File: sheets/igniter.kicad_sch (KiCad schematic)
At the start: 18 parts, among them J18 Screw_Terminal_01x02, J19 Screw_Terminal_01x02, Q2 AO3400A, Q3 AO3400A

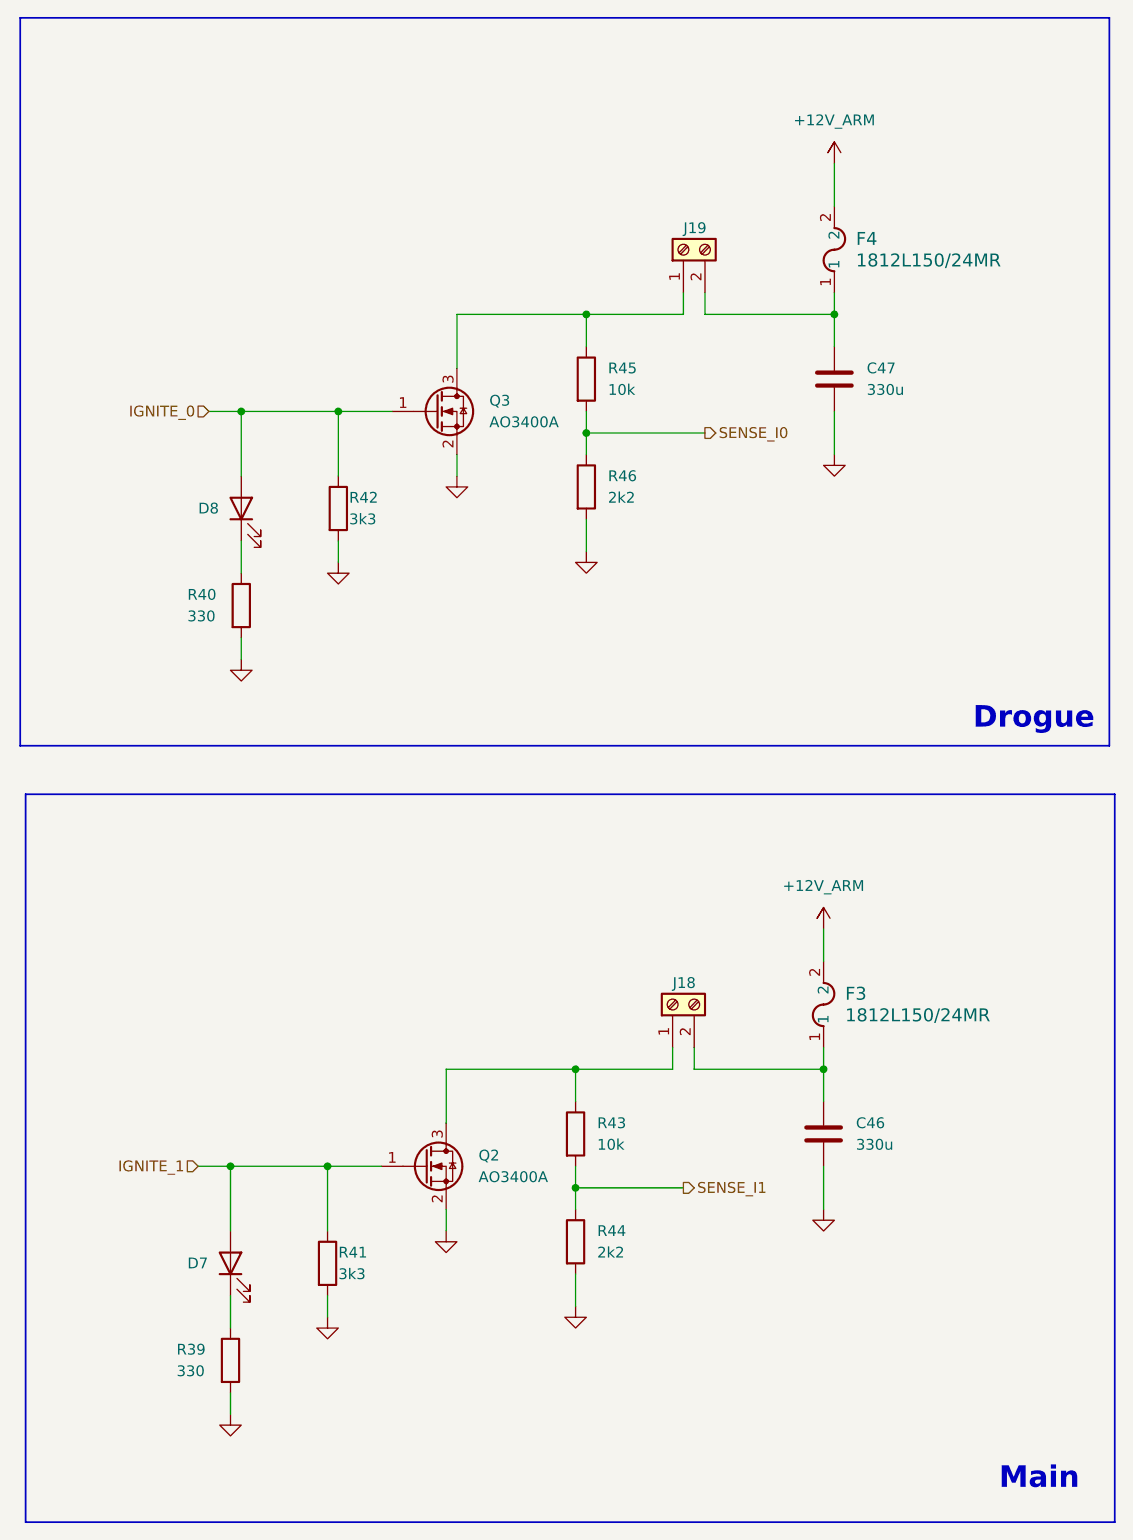
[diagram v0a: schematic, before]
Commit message: updated pyrocircuit with components and TO-252-2 footprint for mosfets. not done with sim
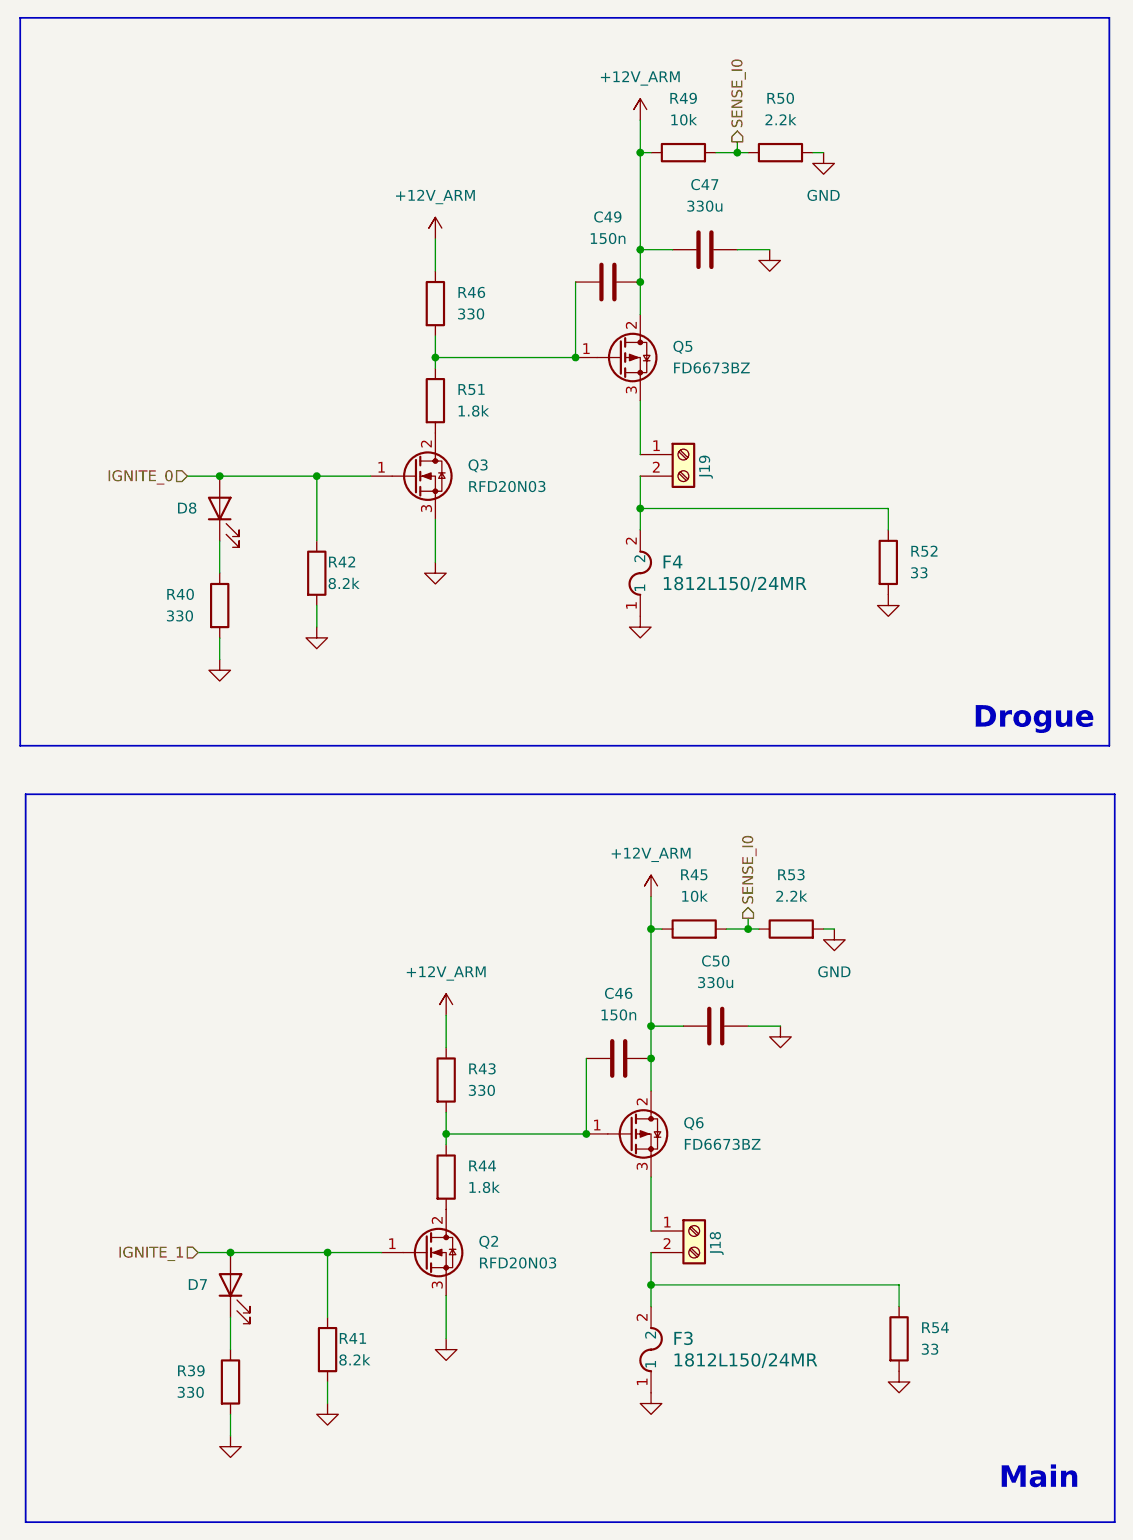
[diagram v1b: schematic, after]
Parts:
- removed Q2, Q3: AO3400A, Package_TO_SOT_SMD:SOT-23, symbol Transistor_FET:AO3400A
- added C49: 150n, symbol Device:C
- added C50: 330u, symbol Device:C
- added Q2, Q3: RFD20N03, Package_TO_SOT_SMD:TO-252-2, symbol Transistor_FET:Q_NMOS_GDS
- added Q5, Q6: FD6673BZ, Package_TO_SOT_SMD:TO-252-2, symbol Transistor_FET:Q_PMOS_GDS
- added R49: 10k, symbol Device:R
- added R50, R53: 2.2k, symbol Device:R
- added R51: 1.8k, symbol Device:R
- added R52, R54: 33, symbol Device:R
- C46: value 330u -> 150n
- R41, R42: value 3k3 -> 8.2k
- R43: value 10k -> 330
- R44: value 2k2 -> 1.8k
- R46: value 2k2 -> 330
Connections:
- net +12V_ARM: now also C46.1, C47.2, R43.1, R45.1, R46.1, C49.1, C50.2, Q5.2 (D), Q6.2 (D), R49.1; no longer F3.2, F4.2
- net GND: now also C47.1, F3.1, F4.1, C50.1, Q2.3 (S), Q3.3 (S), R50.2, R52.2, R53.2, R54.2; no longer C46.2, C47.2, R44.2, R46.2
- net IGNITE_0: now also Q3.1 (G)
- net IGNITE_1: now also Q2.1 (G)
- net SENSE_I0: now also R49.2, R50.1, R53.1; no longer R46.1
- net at J19.1 (Pin_1): now also Q5.3 (S); no longer R45.1
- net at J18.1 (Pin_1): now also Q6.3 (S); no longer R43.1
- net SENSE_I1: no longer names the net of R43.2, R44.1
- net SENSE_I1: now also C46.2, Q6.1 (G)
- new net: F3.2, J18.2 (Pin_2), R54.1
- new net: F4.2, J19.2 (Pin_2), R52.1
- new net: Q2.2 (D), R44.2
- new net: C49.2, Q5.1 (G), R46.2, R51.1
- new net: Q3.2 (D), R51.2
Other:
- moved on the sheet: C47, D8, F4, J19, R40, R42, R46

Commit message: changed nmos and 2 resistors, 3 tests passed
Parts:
- Q2, Q3: value RFD20N03 -> AO3400A
- R43, R46: value 330 -> 1k
- R44, R51: value 1.8k -> 100
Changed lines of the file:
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@@
 			)
 		)
-		(property "Value" "1.8k"
+		(property "Value" "100"
 			(at 69.85 153.6699 0)
 			(effects
@@
 			)
 		)
-		(property "Value" "1.8k"
+		(property "Value" "100"
 			(at 68.58 62.2299 0)
 			(effects
@@
 			)
 		)
-		(property "Value" "RFD20N03"
+		(property "Value" "AO3400A"
 			(at 71.12 162.5599 0)
 			(effects
@@
 			)
 		)
-		(property "Value" "330"
+		(property "Value" "1k"
 			(at 69.85 142.2399 0)
 			(effects
@@
 			)
 		)
-		(property "Value" "RFD20N03"
+		(property "Value" "AO3400A"
 			(at 69.85 71.1199 0)
 			(effects
@@
 			)
 		)
-		(property "Value" "330"
+		(property "Value" "1k"
 			(at 68.58 50.7999 0)
 			(effects

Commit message: removed sense continuity circuit, all tests passed
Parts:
- removed R52, R54: 33, symbol Device:R

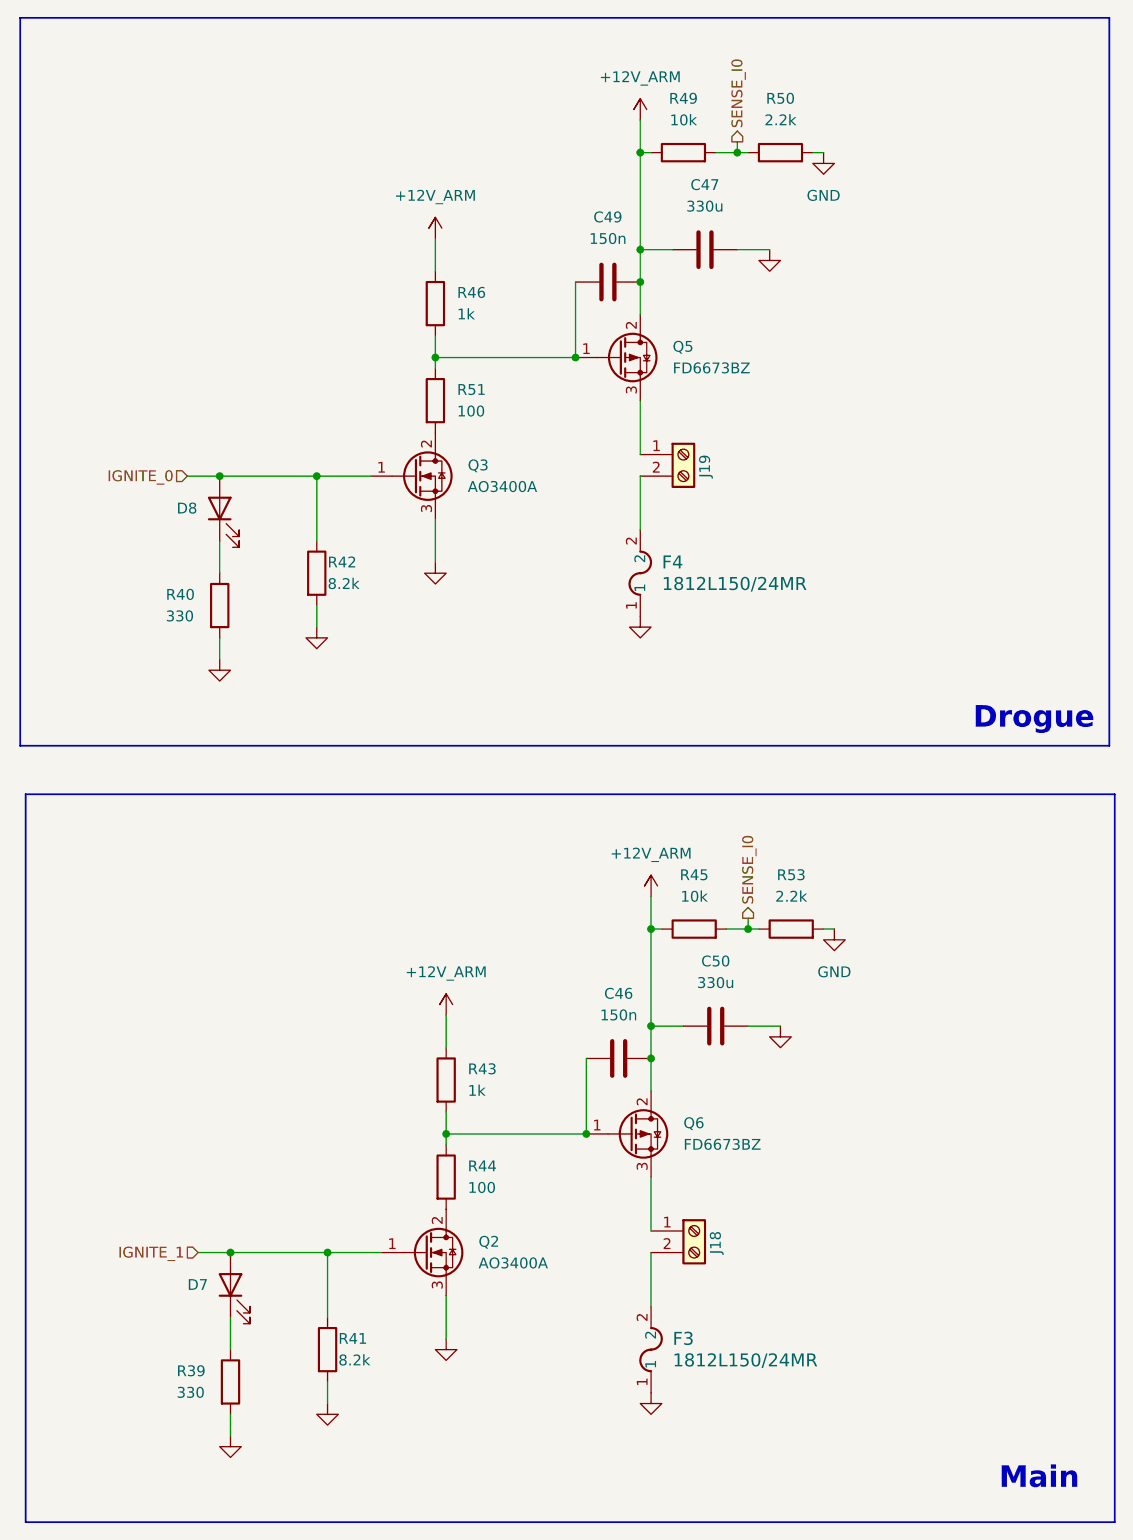
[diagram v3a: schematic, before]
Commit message: added ematch continuity part of circuit, tested
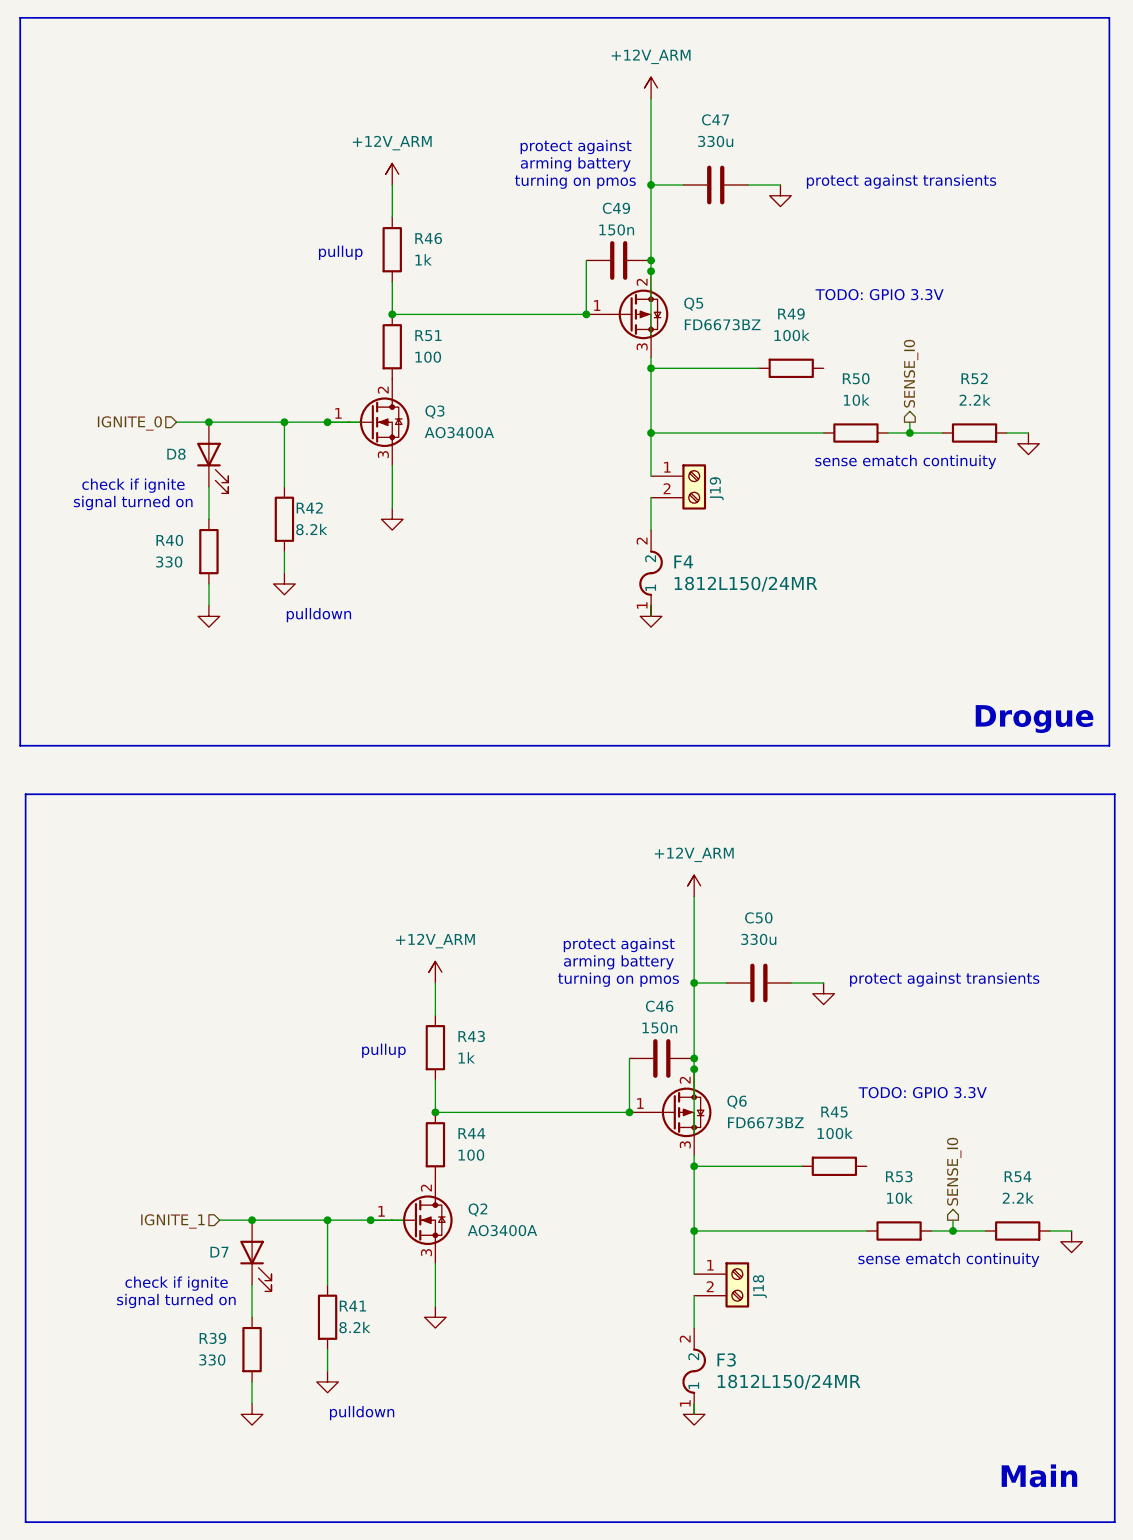
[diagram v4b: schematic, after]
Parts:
- added R52, R54: 2.2k, symbol Device:R
- R45, R49: value 10k -> 100k
- R50, R53: value 2.2k -> 10k
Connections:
- net +12V_ARM: no longer R45.1, R49.1
- net GND: now also R52.2, R54.2; no longer R50.2, R53.2
- net SENSE_I0: now also R50.2, R53.2, R52.1, R54.1; no longer R45.2, R49.2, R50.1, R53.1
- net at J18.1 (Pin_1), Q6.3 (S): now also R45.2, R53.1
- net at J19.1 (Pin_1), Q5.3 (S): now also R49.2, R50.1
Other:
- note added: "TODO: GPIO 3.3V"
- note added: "check if ignite signal turned on"
- note added: "protect against arming battery turning on pmos"
- note added: "protect against transients"
- note added: "pulldown"
- note added: "pullup"
- note added: "sense ematch continuity"
- moved on the sheet: C47, C49, D8, F4, J19, Q3, Q5, R40, R42, R46, R51

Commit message: finalized ematch sensing ciruit, not simmed
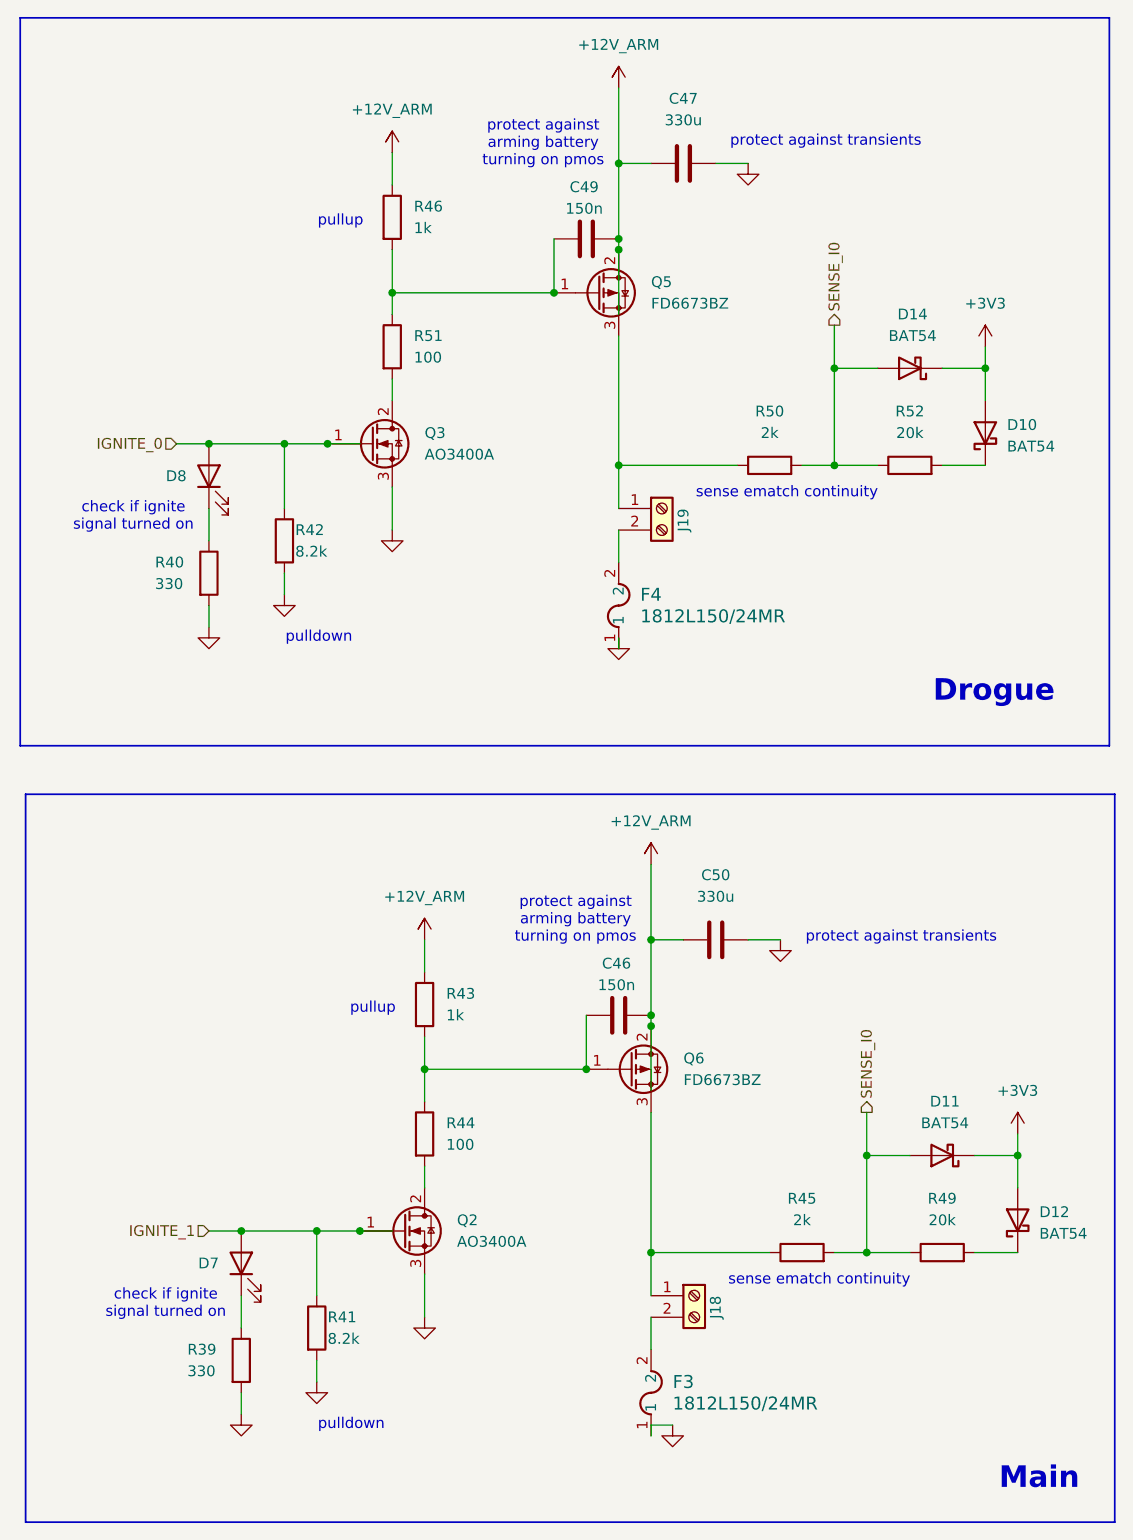
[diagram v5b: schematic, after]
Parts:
- removed R53: 10k, symbol Device:R
- removed R54: 2.2k, symbol Device:R
- added D10, D11, D12, D14: BAT54, Diode_SMD:D_SOD-323F, symbol Diode:BAT54J
- R45: value 100k -> 2k
- R49: value 100k -> 20k
- R50: value 10k -> 2k
- R52: value 2.2k -> 20k
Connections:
- net GND: no longer R52.2
- net SENSE_I0: now also R45.2, R49.1, D11.2 (A), D14.2 (A)
- net at J18.1 (Pin_1), Q6.3 (S): now also R45.1; no longer R45.2
- net at J19.1 (Pin_1), Q5.3 (S), R50.1: no longer R49.2
- new net: D10.1 (K), R52.2
- new net: D12.1 (K), R49.2
- new net +3V3: D10.2 (A), D11.1 (K), D12.2 (A), D14.1 (K)
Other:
- note removed: "TODO: GPIO 3.3V"
- moved on the sheet: C47, C49, D8, F4, J19, Q3, Q5, R40, R42, R46, R50, R52

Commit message: final: passed all tests.
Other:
- note added: "protect against battery arm turning on pmos"
- note added: "protect mcu pins from voltage spike when ematch deploys"
- note removed: "protect against arming battery turning on pmos"
- moved on the sheet: D10, D14, R50, R52
